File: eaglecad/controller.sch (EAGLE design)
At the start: 112 parts, among them J1 CORTEX_DEBUG_PTH, J2 U.FL, J3 U.FL, J4 U.FL, J6 TSV991ILT, J7 TSV991ILT, U2 TCAN330, U3 LM3671MF-3.3, U6 STM32F042K6, X1 16MHZ-2.5x2mm

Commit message: Added the encoder to the schematic. We need to configure the F0 to have a SPI chip select pin to connect to the CSn pin on the encoder.
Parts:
- removed JP4: (no value), adafruit:PINHD-1X8-3.5MM
- added U1: AS5047P, AS5047P:AS5047P
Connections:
- removed net CSN: JP4.5
- removed net MISO: JP4.2
- removed net MOSI: JP4.3
- removed net NC: JP4.6
- removed net SCK: JP4.4
- new net N$9: U1.CSN
- net 3.3V: now also U1.MOSI, U1.VDD, U1.VDD3V; no longer JP4.7, JP4.8
- net GND: now also U1.GND; no longer JP4.1
- net PA5/SPI1_SCK: now also U1.CLK
- net PB4/SPI1_MISO: now also U1.MISO
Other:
- note added: "Encoder"
- note removed: "Encoder Connection"
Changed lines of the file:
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@@
 <part name="R26" library="rcl" library_urn="urn:adsk.eagle:library:334" deviceset="R-US_" device="R0402" package3d_urn="urn:adsk.eagle:package:23547/2" value="330"/>
 <part name="FRAME3" library="frames" library_urn="urn:adsk.eagle:library:229" deviceset="FRAME_B_L" device=""/>
-<part name="JP4" library="adafruit" library_urn="urn:adsk.eagle:library:420" deviceset="PINHD-1X8" device="-3.5MM"/>
-<part name="SUPPLY22" library="SparkFun-PowerSymbols" library_urn="urn:adsk.eagle:library:530" deviceset="3.3V" device=""/>
-<part name="GND48" library="supply1" library_urn="urn:adsk.eagle:library:371" deviceset="GND" device=""/>
 <part name="J6" library="TSV991ILT" deviceset="TSV991ILT" device=""/>
 <part name="GND38" library="supply1" library_urn="urn:adsk.eagle:library:371" deviceset="GND" device=""/>
@@
 <part name="D5" library="adafruit" library_urn="urn:adsk.eagle:library:420" deviceset="DIODE" device="SMA"/>
 <part name="SUPPLY23" library="SparkFun-PowerSymbols" library_urn="urn:adsk.eagle:library:530" deviceset="3.3V" device=""/>
+<part name="U1" library="AS5047P" deviceset="AS5047P" device=""/>
+<part name="SUPPLY24" library="SparkFun-PowerSymbols" library_urn="urn:adsk.eagle:library:530" deviceset="3.3V" device=""/>
+<part name="GND57" library="supply1" library_urn="urn:adsk.eagle:library:371" deviceset="GND" device=""/>
+<part name="SUPPLY22" library="SparkFun-PowerSymbols" library_urn="urn:adsk.eagle:library:530" deviceset="3.3V" device=""/>
+<part name="FRAME4" library="frames" library_urn="urn:adsk.eagle:library:229" deviceset="FRAME_B_L" device=""/>
 </parts>
 <sheets>
@@
 <segment>
 <pinref part="U6" gate="G$1" pin="PA6"/>
-<label x="245.11" y="137.16" size="1.778" layer="95" rot="MR0"/>
+<label x="246.634" y="137.16" size="1.778" layer="95" rot="MR0"/>
 <wire x1="248.92" y1="137.16" x2="228.6" y2="137.16" width="0.1524" layer="91"/>
 </segment>
@@
 <sheet>
 <plain>
-<text x="-20.32" y="63.5" size="5.08" layer="97">Encoder Connection</text>
+<text x="200.66" y="185.42" size="5.08" layer="97">Encoder</text>
 </plain>
 <instances>
-<instance part="JP4" gate="G$1" x="2.54" y="38.1" rot="R180"/>
-<instance part="SUPPLY22" gate="G$1" x="15.24" y="53.34"/>
-<instance part="GND48" gate="1" x="12.7" y="22.86"/>
+<instance part="U1" gate="G$1" x="213.36" y="149.86"/>
+<instance part="SUPPLY24" gate="G$1" x="243.84" y="187.96"/>
+<instance part="GND57" gate="1" x="238.76" y="121.92"/>
+<instance part="SUPPLY22" gate="G$1" x="160.02" y="182.88"/>
+<instance part="FRAME4" gate="G$1" x="0" y="0"/>
+<instance part="FRAME4" gate="G$2" x="325.12" y="0"/>
 </instances>
 <busses>
 </busses>
 <nets>
+<net name="3.3V" class="0">
+<segment>
+<pinref part="U1" gate="G$1" pin="VDD3V"/>
+<wire x1="231.14" y1="154.94" x2="243.84" y2="154.94" width="0.1524" layer="91"/>
+<pinref part="U1" gate="G$1" pin="VDD"/>
+<wire x1="231.14" y1="149.86" x2="243.84" y2="149.86" width="0.1524" layer="91"/>
+<wire x1="243.84" y1="149.86" x2="243.84" y2="154.94" width="0.1524" layer="91"/>
+<pinref part="SUPPLY24" gate="G$1" pin="3.3V"/>
+<wire x1="243.84" y1="154.94" x2="243.84" y2="187.96" width="0.1524" layer="91"/>
+<junction x="243.84" y="154.94"/>
+</segment>
+<segment>
+<pinref part="U1" gate="G$1" pin="MOSI"/>
+<wire x1="195.58" y1="149.86" x2="160.02" y2="149.86" width="0.1524" layer="91"/>
+<wire x1="160.02" y1="149.86" x2="160.02" y2="182.88" width="0.1524" layer="91"/>
+<pinref part="SUPPLY22" gate="G$1" pin="3.3V"/>
+</segment>
+</net>
 <net name="GND" class="0">
 <segment>
-<pinref part="JP4" gate="G$1" pin="1"/>
-<wire x1="5.08" y1="30.48" x2="12.7" y2="30.48" width="0.1524" layer="91"/>
-<wire x1="12.7" y1="30.48" x2="12.7" y2="25.4" width="0.1524" layer="91"/>
-<pinref part="GND48" gate="1" pin="GND"/>
-</segment>
-</net>
-<net name="3.3V" class="0">
-<segment>
-<pinref part="JP4" gate="G$1" pin="7"/>
-<wire x1="5.08" y1="45.72" x2="15.24" y2="45.72" width="0.1524" layer="91"/>
-<pinref part="JP4" gate="G$1" pin="8"/>
-<wire x1="15.24" y1="45.72" x2="15.24" y2="48.26" width="0.1524" layer="91"/>
-<wire x1="15.24" y1="48.26" x2="5.08" y2="48.26" width="0.1524" layer="91"/>
-<wire x1="15.24" y1="48.26" x2="15.24" y2="53.34" width="0.1524" layer="91"/>
-<junction x="15.24" y="48.26"/>
-<pinref part="SUPPLY22" gate="G$1" pin="3.3V"/>
-</segment>
-</net>
-<net name="CSN" class="0">
-<segment>
-<pinref part="JP4" gate="G$1" pin="5"/>
-<wire x1="5.08" y1="40.64" x2="17.78" y2="40.64" width="0.1524" layer="91"/>
-<label x="17.78" y="40.64" size="1.778" layer="95"/>
-</segment>
-</net>
-<net name="SCK" class="0">
-<segment>
-<pinref part="JP4" gate="G$1" pin="4"/>
-<wire x1="5.08" y1="38.1" x2="17.78" y2="38.1" width="0.1524" layer="91"/>
-<label x="17.78" y="38.1" size="1.778" layer="95"/>
-</segment>
-</net>
-<net name="MOSI" class="0">
-<segment>
-<pinref part="JP4" gate="G$1" pin="3"/>
-<wire x1="5.08" y1="35.56" x2="17.78" y2="35.56" width="0.1524" layer="91"/>
-<label x="17.78" y="35.56" size="1.778" layer="95"/>
-</segment>
-</net>
-<net name="MISO" class="0">
-<segment>
-<pinref part="JP4" gate="G$1" pin="2"/>
-<wire x1="5.08" y1="33.02" x2="17.78" y2="33.02" width="0.1524" layer="91"/>
-<label x="17.78" y="33.02" size="1.778" layer="95"/>
-</segment>
-</net>
-<net name="NC" class="0">
-<segment>
-<pinref part="JP4" gate="G$1" pin="6"/>
-<wire x1="5.08" y1="43.18" x2="12.7" y2="43.18" width="0.1524" layer="91"/>
-<label x="12.7" y="43.18" size="1.778" layer="95"/>
-</segment>
-</net>
+<pinref part="U1" gate="G$1" pin="GND"/>
+<wire x1="231.14" y1="160.02" x2="238.76" y2="160.02" width="0.1524" layer="91"/>
+<wire x1="238.76" y1="160.02" x2="238.76" y2="124.46" width="0.1524" layer="91"/>
+<pinref part="GND57" gate="1" pin="GND"/>
+</segment>
+</net>
+<net name="PA5/SPI1_SCK" class="0">
+<segment>
+<pinref part="U1" gate="G$1" pin="CLK"/>
+<wire x1="195.58" y1="160.02" x2="185.42" y2="160.02" width="0.1524" layer="91"/>
+<label x="172.72" y="160.02" size="1.778" layer="95"/>
+</segment>
+</net>
+<net name="PB4/SPI1_MISO" class="0">
+<segment>
+<pinref part="U1" gate="G$1" pin="MISO"/>
+<wire x1="195.58" y1="154.94" x2="185.42" y2="154.94" width="0.1524" layer="91"/>
+<label x="172.72" y="154.94" size="1.778" layer="95"/>
+</segment>
+</net>
+<net name="N$9" class="0">
+<segment>
+<pinref part="U1" gate="G$1" pin="CSN"/>
+<wire x1="195.58" y1="165.1" x2="185.42" y2="165.1" width="0.1524" layer="91"/>
+</segment>
+</net>

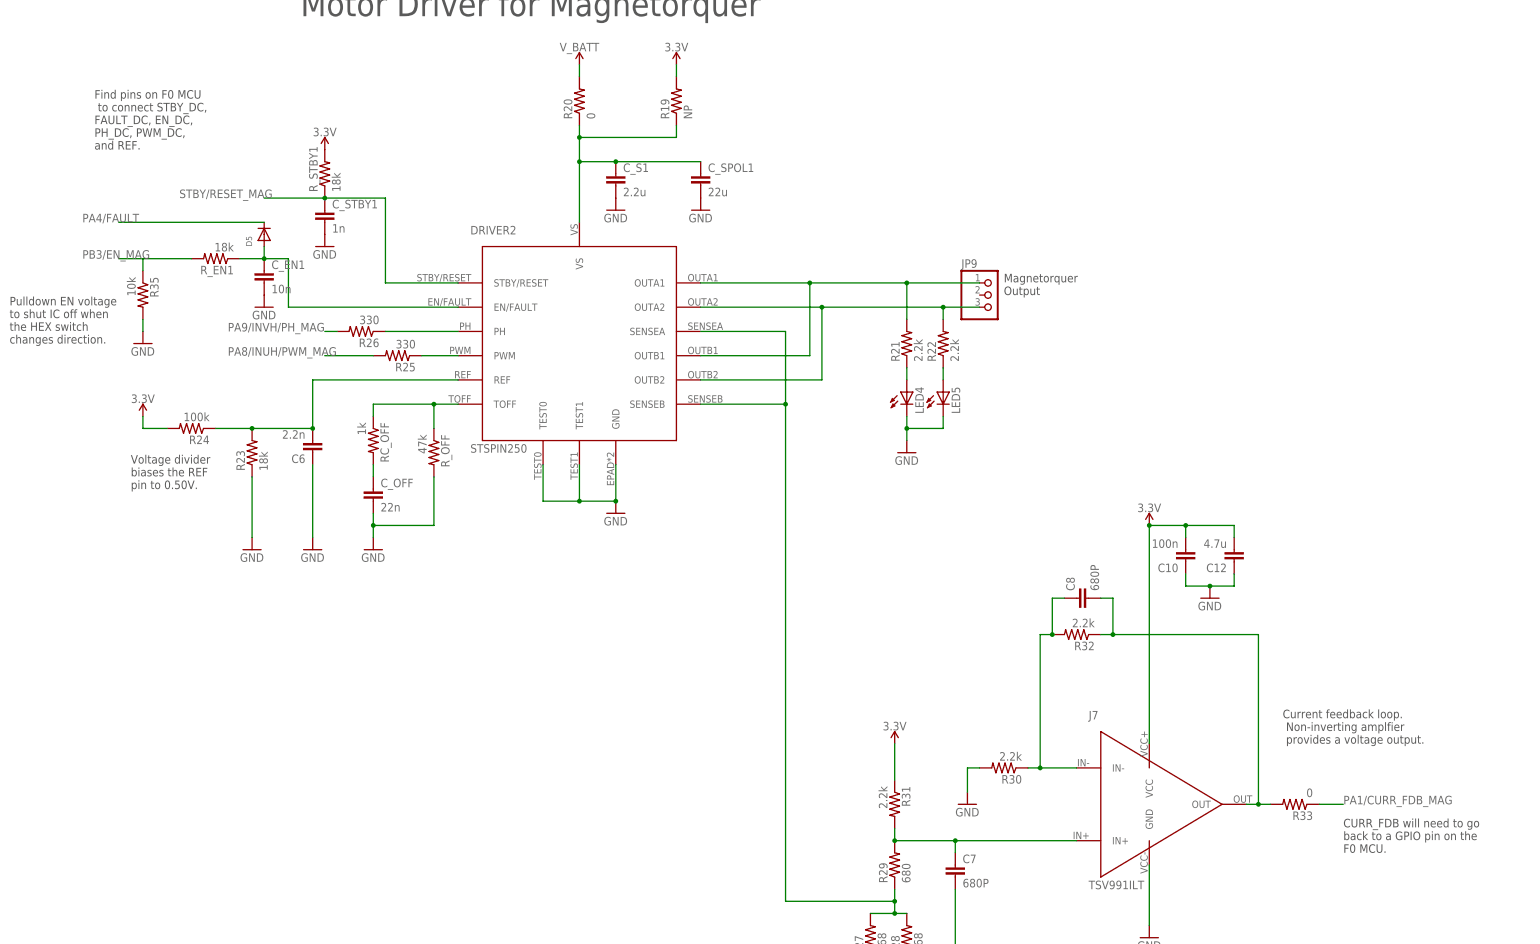
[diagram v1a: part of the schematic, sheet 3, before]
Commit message: Removed unneeded text and did some cleanup. Everything looks good except the encoder has a CSn pin that needs to connect to the F0 MCU somehow. The CSn pin is for SPI chip select. Where do we connect this?
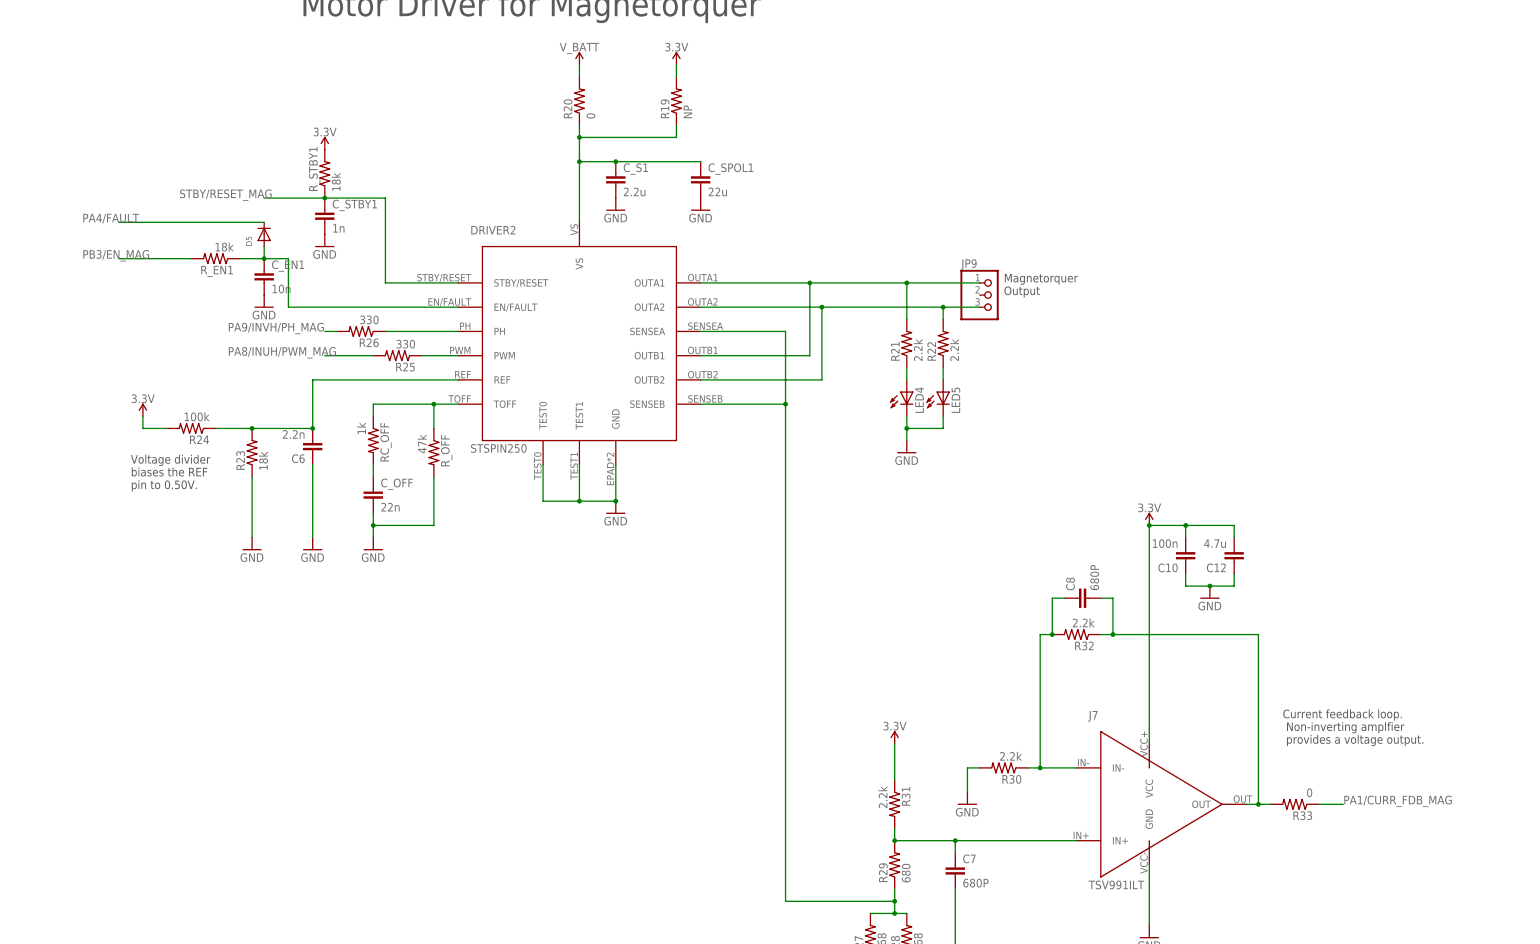
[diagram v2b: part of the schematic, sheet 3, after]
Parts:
- removed R34, R35: 10k, rcl:R-US_R0402
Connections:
- removed net EN_BLDC1: R35.1
- net GND: no longer R34.2, R35.2
- net PA15/EN_BLDC: no longer R34.1
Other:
- note added: "CAN_SHDN and CAN_LSTN pins have internal pull-down resistors. If CAN_SHDN is pulled high it shuts the IC off. If CAN_LSTN is pulled high it puts the IC intro receive-only mode. Leave CAN_SHDN disconnected."
- note added: "What do we connect the CSn pin to? This is for SPI chip select."
- note removed: "CAN_SHDN and CAN_LSTN pins have internal pull-down resistors. If CAN_SHDN is pulled high it shuts the IC off. If CAN_LSTN is pulled high it puts the IC intro receive-only mode. Just leave these disconnected."
- note removed: "CURR_FDB will need to go back to a GPIO pin on the F0 MCU."
- note removed: "Find pins on F0 MCU to connect STBY_DC, FAULT_DC, EN_DC, PH_DC, PWM_DC, and REF."
- note removed: "Pulldown EN voltage to shut IC off when the HEX switch changes direction."
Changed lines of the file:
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@@
 <part name="GND55" library="supply1" library_urn="urn:adsk.eagle:library:371" deviceset="GND" device=""/>
 <part name="GND56" library="supply1" library_urn="urn:adsk.eagle:library:371" deviceset="GND" device=""/>
-<part name="R34" library="rcl" library_urn="urn:adsk.eagle:library:334" deviceset="R-US_" device="R0402" package3d_urn="urn:adsk.eagle:package:23547/2" value="10k"/>
-<part name="GND59" library="supply1" library_urn="urn:adsk.eagle:library:371" deviceset="GND" device=""/>
-<part name="R35" library="rcl" library_urn="urn:adsk.eagle:library:334" deviceset="R-US_" device="R0402" package3d_urn="urn:adsk.eagle:package:23547/2" value="10k"/>
-<part name="GND60" library="supply1" library_urn="urn:adsk.eagle:library:371" deviceset="GND" device=""/>
 <part name="D4" library="adafruit" library_urn="urn:adsk.eagle:library:420" deviceset="DIODE" device="SMA"/>
 <part name="D5" library="adafruit" library_urn="urn:adsk.eagle:library:420" deviceset="DIODE" device="SMA"/>
@@
 If CAN_LSTN is pulled high
 it puts the IC intro receive-only
-mode. Just leave these
-disconnected.</text>
+mode. Leave CAN_SHDN
+ disconnected.</text>
 </plain>
 <instances>
@@
  Non-inverting amplfier
  provides a voltage output.</text>
-<text x="302.26" y="83.82" size="1.778" layer="97">CURR_FDB will need to go
-back to a GPIO pin on the
-F0 MCU.</text>
 <text x="116.84" y="241.3" size="5.08" layer="97">Motor Driver for BLDC</text>
-<text x="43.18" y="177.8" size="1.778" layer="97">Pulldown EN voltage
-to shut IC off when
-the HEX switch
-changes direction.</text>
 </plain>
 <instances>
@@
 <instance part="GND38" gate="1" x="208.28" y="53.34"/>
 <instance part="GND54" gate="1" x="223.52" y="93.98"/>
-<instance part="R34" gate="G$1" x="71.12" y="187.96" rot="R270"/>
-<instance part="GND59" gate="1" x="71.12" y="177.8"/>
 <instance part="D4" gate="G$1" x="96.52" y="198.12" rot="R90"/>
 </instances>
@@
 <pinref part="GND40" gate="1" pin="GND"/>
 <wire x1="261.62" y1="81.28" x2="261.62" y2="68.58" width="0.1524" layer="91"/>
-</segment>
-<segment>
-<pinref part="GND59" gate="1" pin="GND"/>
-<pinref part="R34" gate="G$1" pin="2"/>
-<wire x1="71.12" y1="180.34" x2="71.12" y2="182.88" width="0.1524" layer="91"/>
 </segment>
 </net>
@@
 <segment>
 <pinref part="R_EN" gate="G$1" pin="2"/>
-<wire x1="81.28" y1="195.58" x2="71.12" y2="195.58" width="0.1524" layer="91"/>
+<wire x1="81.28" y1="195.58" x2="66.04" y2="195.58" width="0.1524" layer="91"/>
 <label x="60.96" y="195.58" size="1.778" layer="95"/>
-<pinref part="R34" gate="G$1" pin="1"/>
-<wire x1="71.12" y1="195.58" x2="66.04" y2="195.58" width="0.1524" layer="91"/>
-<wire x1="71.12" y1="193.04" x2="71.12" y2="195.58" width="0.1524" layer="91"/>
-<junction x="71.12" y="195.58"/>
 </segment>
 </net>
@@
 <text x="231.14" y="198.12" size="1.778" layer="97">Magnetorquer
 Output</text>
-<text x="40.64" y="228.6" size="1.778" layer="97">Find pins on F0 MCU
- to connect STBY_DC,
-FAULT_DC, EN_DC,
-PH_DC, PWM_DC,
-and REF.</text>
 <text x="83.82" y="256.54" size="5.08" layer="97">Motor Driver for Magnetorquer</text>
 <text x="289.56" y="104.14" size="1.778" layer="97">Current feedback loop.
  Non-inverting amplfier
  provides a voltage output.</text>
-<text x="302.26" y="81.28" size="1.778" layer="97">CURR_FDB will need to go
-back to a GPIO pin on the
-F0 MCU.</text>
-<text x="22.86" y="187.96" size="1.778" layer="97">Pulldown EN voltage
-to shut IC off when
-the HEX switch
-changes direction.</text>
 <text x="48.26" y="157.48" size="1.778" layer="97">Voltage divider
 biases the REF
@@
 <instance part="GND55" gate="1" x="208.28" y="50.8"/>
 <instance part="GND56" gate="1" x="223.52" y="91.44"/>
-<instance part="R35" gate="G$1" x="50.8" y="198.12" rot="R270"/>
-<instance part="GND60" gate="1" x="50.8" y="187.96"/>
 <instance part="D5" gate="G$1" x="76.2" y="210.82" rot="R90"/>
 <instance part="SUPPLY23" gate="G$1" x="50.8" y="172.72"/>
@@
 <pinref part="GND52" gate="1" pin="GND"/>
 <wire x1="261.62" y1="78.74" x2="261.62" y2="66.04" width="0.1524" layer="91"/>
-</segment>
-<segment>
-<pinref part="GND60" gate="1" pin="GND"/>
-<pinref part="R35" gate="G$1" pin="2"/>
-<wire x1="50.8" y1="190.5" x2="50.8" y2="193.04" width="0.1524" layer="91"/>
 </segment>
 </net>
@@
 </segment>
 </net>
-<net name="EN_BLDC1" class="0">
-<segment>
-<pinref part="R35" gate="G$1" pin="1"/>
-<wire x1="50.8" y1="203.2" x2="50.8" y2="205.74" width="0.1524" layer="91"/>
-</segment>
-</net>
 <net name="PA1/CURR_FDB_MAG" class="0">
 <segment>
@@
 <plain>
 <text x="200.66" y="185.42" size="5.08" layer="97">Encoder</text>
+<text x="167.64" y="172.72" size="1.778" layer="97">What do we connect the
+CSn pin to? This is for
+SPI chip select.</text>
 </plain>
 <instances>

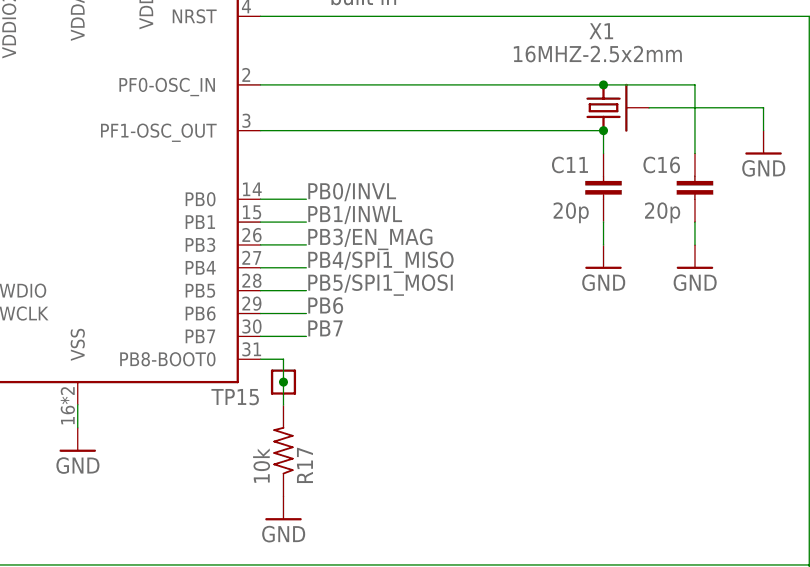
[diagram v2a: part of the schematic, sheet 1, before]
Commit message: Ran ERC, fixed some things and approved some things.
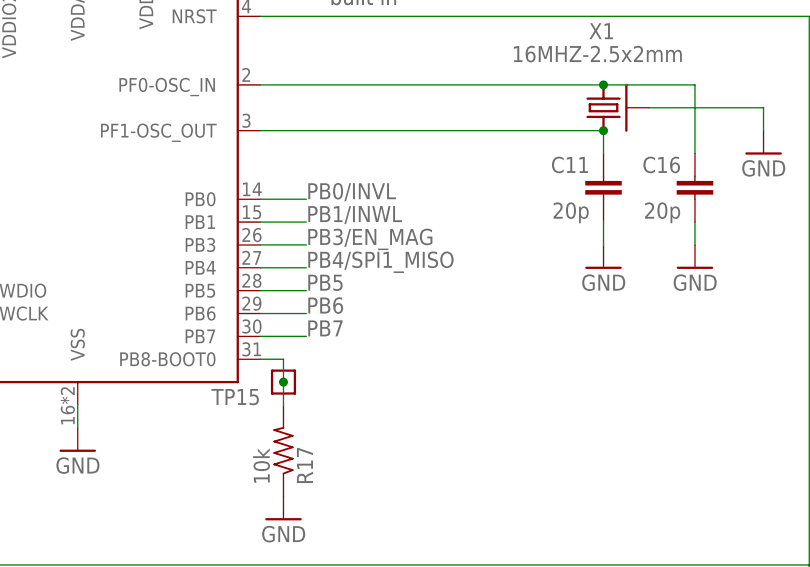
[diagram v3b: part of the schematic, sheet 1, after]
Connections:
- net PB5/SPI1_MOSI renamed PB5
- removed net PA9/INVH: DRIVER1.INVH
- new net EN/FAULT: C_EN.1, D4.A, DRIVER1.EN/FAULT, R_EN.1
- net PA4/FAULT: no longer C_EN.1, D4.A, DRIVER1.EN/FAULT, R_EN.1
- net PA9/INVH/PH_MAG: now also DRIVER1.INVH
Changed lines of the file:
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@@
 </segment>
 </net>
-<net name="PB5/SPI1_MOSI" class="0">
+<net name="PB5" class="0">
 <segment>
 <pinref part="U6" gate="G$1" pin="PB5"/>
@@
 </segment>
 </net>
-<net name="PA9/INVH" class="0">
+<net name="PA9/INVH/PH_MAG" class="0">
 <segment>
 <pinref part="DRIVER1" gate="G$1" pin="INVH"/>
 <wire x1="134.62" y1="180.34" x2="116.84" y2="180.34" width="0.1524" layer="91"/>
-<label x="116.84" y="180.34" size="1.778" layer="95"/>
+<label x="106.68" y="180.34" size="1.778" layer="95"/>
 </segment>
 </net>
@@
 </net>
 <net name="PA4/FAULT" class="0">
+<segment>
+<pinref part="D4" gate="G$1" pin="C"/>
+<wire x1="96.52" y1="200.66" x2="63.5" y2="200.66" width="0.1524" layer="91"/>
+<label x="60.96" y="200.66" size="1.778" layer="95"/>
+</segment>
+</net>
+<net name="PA15/EN_BLDC" class="0">
+<segment>
+<pinref part="R_EN" gate="G$1" pin="2"/>
+<wire x1="81.28" y1="195.58" x2="66.04" y2="195.58" width="0.1524" layer="91"/>
+<label x="60.96" y="195.58" size="1.778" layer="95"/>
+</segment>
+</net>
+<net name="EN/FAULT" class="0">
 <segment>
 <pinref part="R_EN" gate="G$1" pin="1"/>
@@
 <pinref part="D4" gate="G$1" pin="A"/>
 </segment>
-<segment>
-<pinref part="D4" gate="G$1" pin="C"/>
-<wire x1="96.52" y1="200.66" x2="63.5" y2="200.66" width="0.1524" layer="91"/>
-<label x="60.96" y="200.66" size="1.778" layer="95"/>
-</segment>
-</net>
-<net name="PA15/EN_BLDC" class="0">
-<segment>
-<pinref part="R_EN" gate="G$1" pin="2"/>
-<wire x1="81.28" y1="195.58" x2="66.04" y2="195.58" width="0.1524" layer="91"/>
-<label x="60.96" y="195.58" size="1.778" layer="95"/>
-</segment>
-</net>
+</net>
